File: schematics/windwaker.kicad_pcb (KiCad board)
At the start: 2 copper layers, 2 parts, among them U1 WEMOS_C3_mini, U2 This should be a tft later

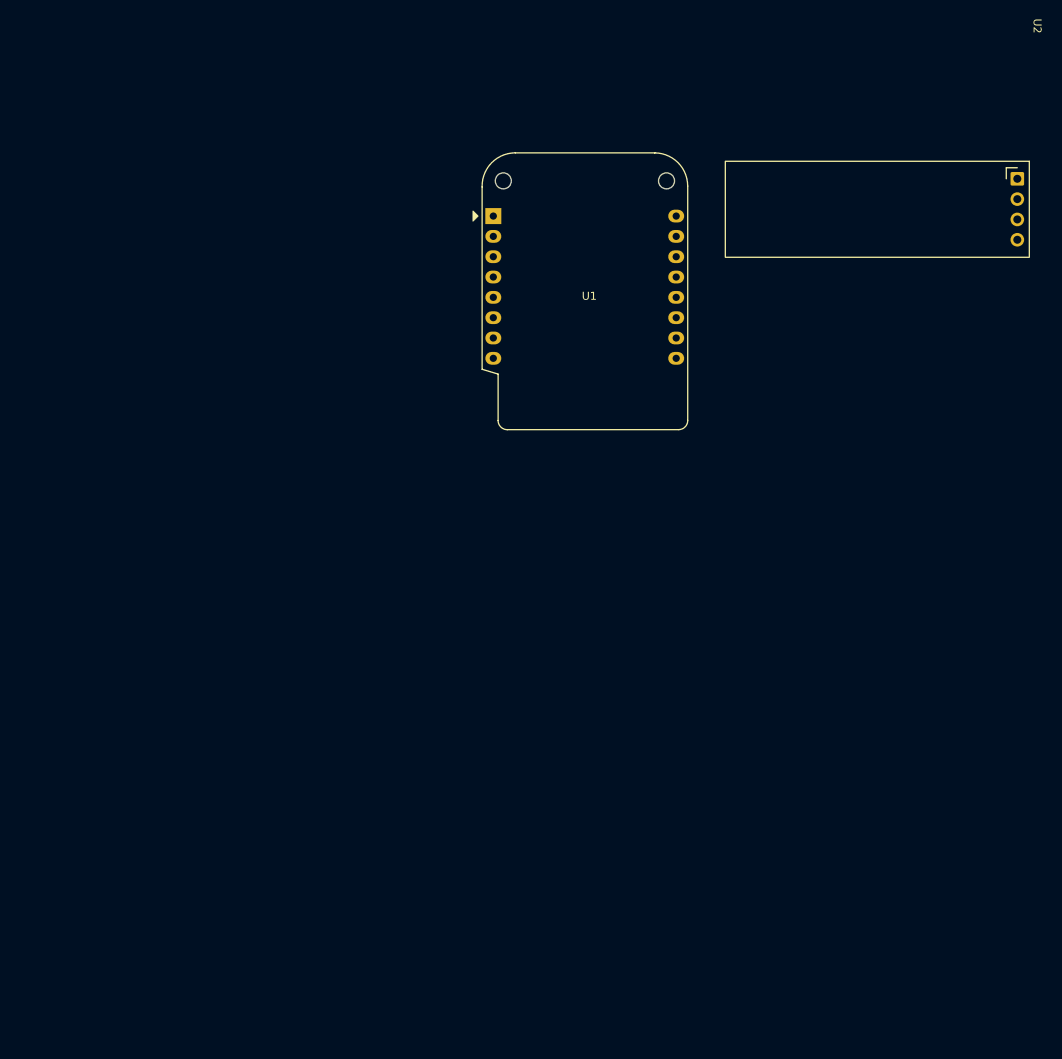
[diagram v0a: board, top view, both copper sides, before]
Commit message: wow, a rough sketch, and a real footprint!
rough sketch by me and footprint for the thing. basic routing can happen now
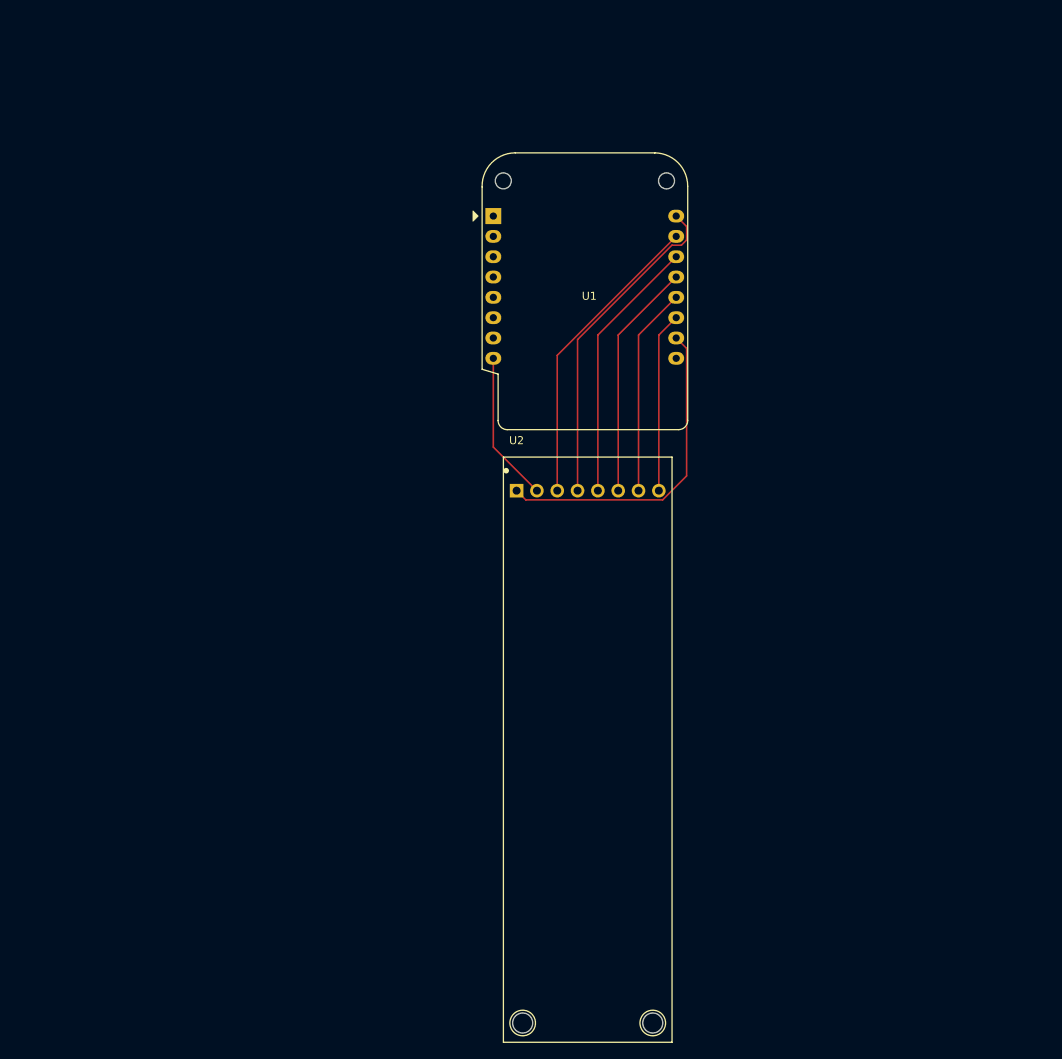
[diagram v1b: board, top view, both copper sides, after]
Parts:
- U2: value This should be a tft later -> TFT Display; footprint Display:ER_OLEDM0.91_1x-I2C -> my_custom_library:TFT-Display_ST7789_2.25in_76x284_8P
- moved U2 73.7 mm to (140.4, 114.7), turned to 0 degrees
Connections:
- U1 pad 10: Net-(BZ1--) -> GND
- U1 pad 11: unconnected-(U1-D6-Pad11) -> Net-(U1-D6)
- U1 pad 12: unconnected-(U1-D7-Pad12) -> Net-(U1-D7)
- U1 pad 13: unconnected-(U1-D8-Pad13) -> Net-(U1-D8)
- U1 pad 14: unconnected-(U1-D10-Pad14) -> Net-(U1-D10)
- U1 pad 8: Net-(BZ1-+) -> +3V3
- U2 pad 1: +3V3 -> GND
- U2 pad 2: GND -> +3V3
- U2 pad 3: Net-(U1-TX) -> Net-(U1-RX)
- U2 pad 4: Net-(U1-RX) -> Net-(U1-TX)
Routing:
- net Net-(U1-TX): track 0.00 -> 41.2 mm
- net GND: track 0.00 -> 40.7 mm
- net Net-(U1-RX): track 0.00 -> 37.9 mm
- net Net-(U1-D10): track 0.00 -> 33.3 mm
- net Net-(U1-D8): track 0.00 -> 29.7 mm
- net Net-(U1-D7): track 0.00 -> 26.1 mm
- net Net-(U1-D6): track 0.00 -> 22.5 mm
- net +3V3: track 0.00 -> 18.8 mm

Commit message: adding some 3d models and routing the pcb
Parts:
- added BZ1: Buzzer, my_custom_library:Buzzer_12x9.5RM7.6, F.Cu at (87.3, 153.2)
- added SW1: SW_Push, Button_Switch_Keyboard:SW_Cherry_MX_1.00u_PCB, F.Cu at (90.0, 130.3)
- added SW2: SW_Push, Button_Switch_Keyboard:SW_Cherry_MX_1.00u_PCB, F.Cu at (90.0, 111.3)
- added SW3: SW_Push, Button_Switch_Keyboard:SW_Cherry_MX_1.00u_PCB, F.Cu at (90.0, 92.2)
- added SW4: SW_Push, Button_Switch_Keyboard:SW_Cherry_MX_1.00u_PCB, F.Cu at (90.0, 73.3)
- U1: moved to B.Cu
- moved U1 40.9 mm to (99.4, 95.2)
- moved U2 37.3 mm to (119.7, 145.8), turned to 180 degrees
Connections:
- U1 pad 3: unconnected-(U1-D2-Pad3) -> Net-(U1-D2)
- U1 pad 4: unconnected-(U1-D1-Pad4) -> Net-(U1-D1)
- U1 pad 5: unconnected-(U1-D0-Pad5) -> Net-(U1-D0)
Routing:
- net GND: track 40.7 -> 161.7 mm
- net +3V3: track 18.8 -> 127.1 mm
- net Net-(U1-D6): track 22.5 -> 71.7 mm
- net Net-(U1-D7): track 26.1 -> 68.1 mm
- net Net-(U1-D3): track 0.00 -> 41.5 mm
- net Net-(U1-D8): track 29.7 -> 64.5 mm
- net Net-(U1-D10): track 33.3 -> 60.9 mm
- net Net-(U1-D2): track 0.00 -> 25.9 mm
- net Net-(U1-RX): track 37.9 -> 56.3 mm
- net Net-(U1-D0): track 0.00 -> 15.7 mm
- net Net-(U1-TX): track 41.2 -> 54.8 mm
- net Net-(U1-D1): track 0.00 -> 11.3 mm
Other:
- board outline added: 46.4 x 93.6 mm

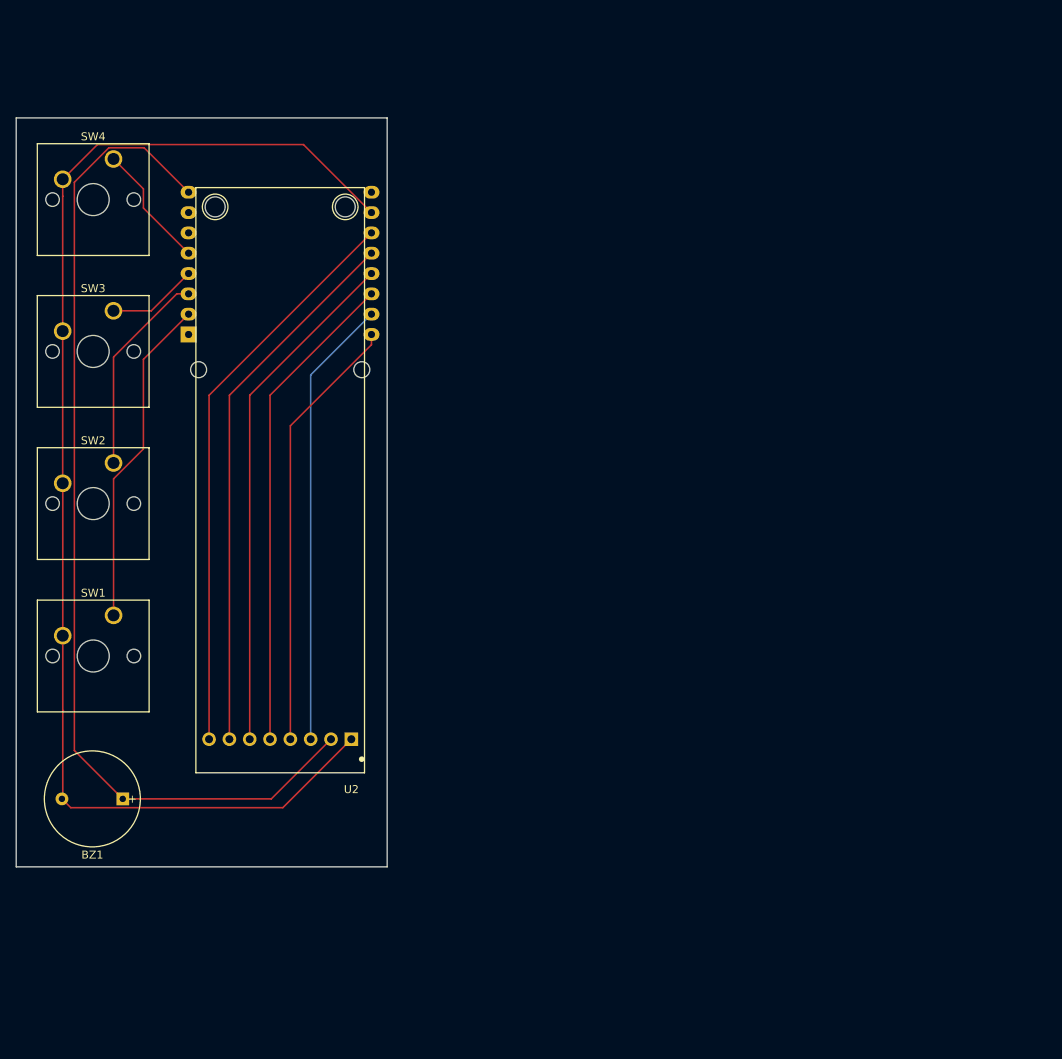
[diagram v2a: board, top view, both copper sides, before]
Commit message: Begin journaling and firmware work
Firmware now has cpp classes for the mx switches,  and a wiring diagram
Also changed up .gitignore to be from the KiCad gitnore from official Github, now containing the .history folder (no more of those yes).
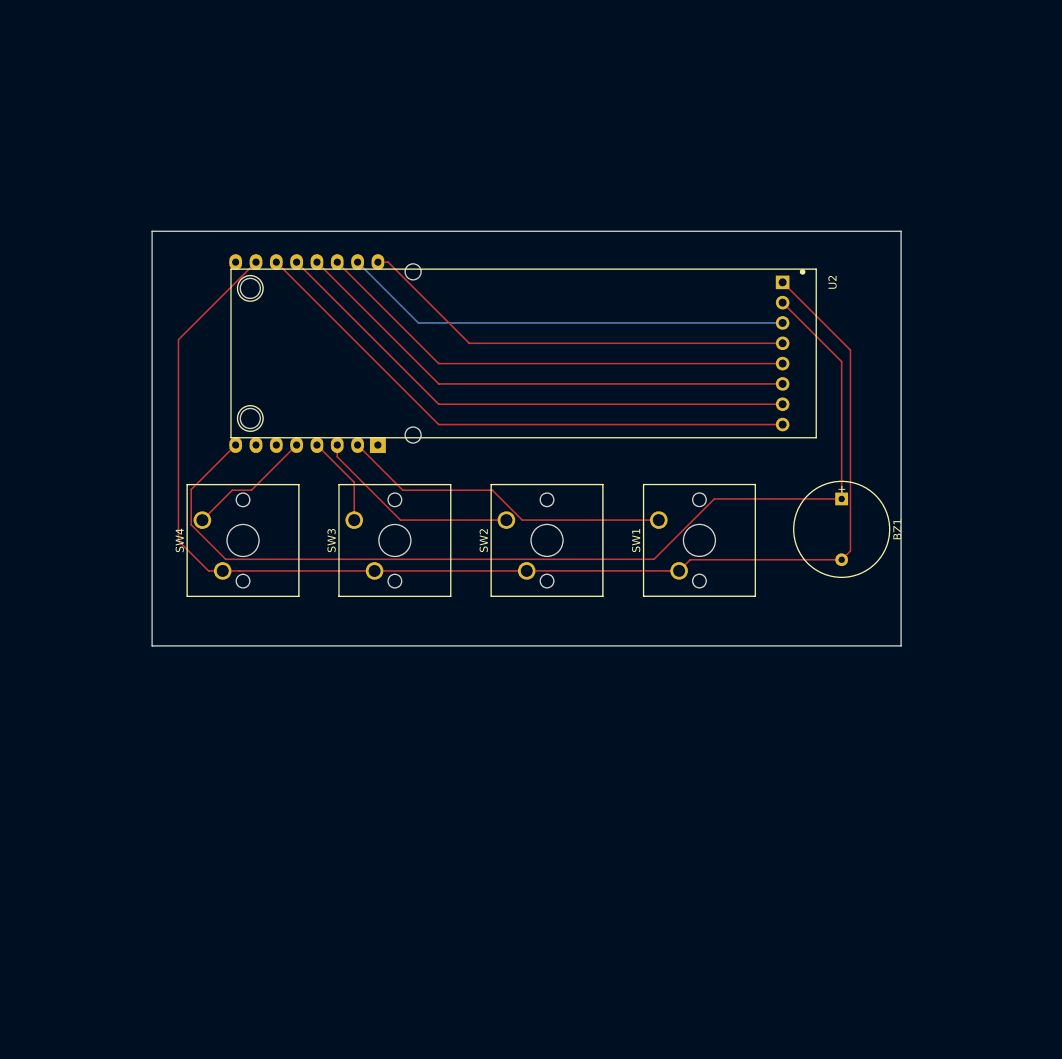
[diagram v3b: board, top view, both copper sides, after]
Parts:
- moved BZ1 99.5 mm to (181.0, 119.6), turned to -90 degrees
- moved U2 78.5 mm to (173.6, 88.7), turned to -90 degrees
- moved SW1 69.2 mm to (158.1, 118.4), turned to 90 degrees
- moved SW2 49.6 mm to (139.1, 118.4), turned to 90 degrees
- moved SW4 46.5 mm to (101.1, 118.4), turned to 90 degrees
- moved SW3 39.9 mm to (120.1, 118.4), turned to 90 degrees
- moved U1 27.4 mm to (123.0, 109.0), turned to 90 degrees
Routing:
- net +3V3: track 127.1 -> 126.1 mm
- net GND: track 161.7 -> 162.5 mm
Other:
- board size 46.4 x 93.6 mm -> 93.6 x 51.8 mm

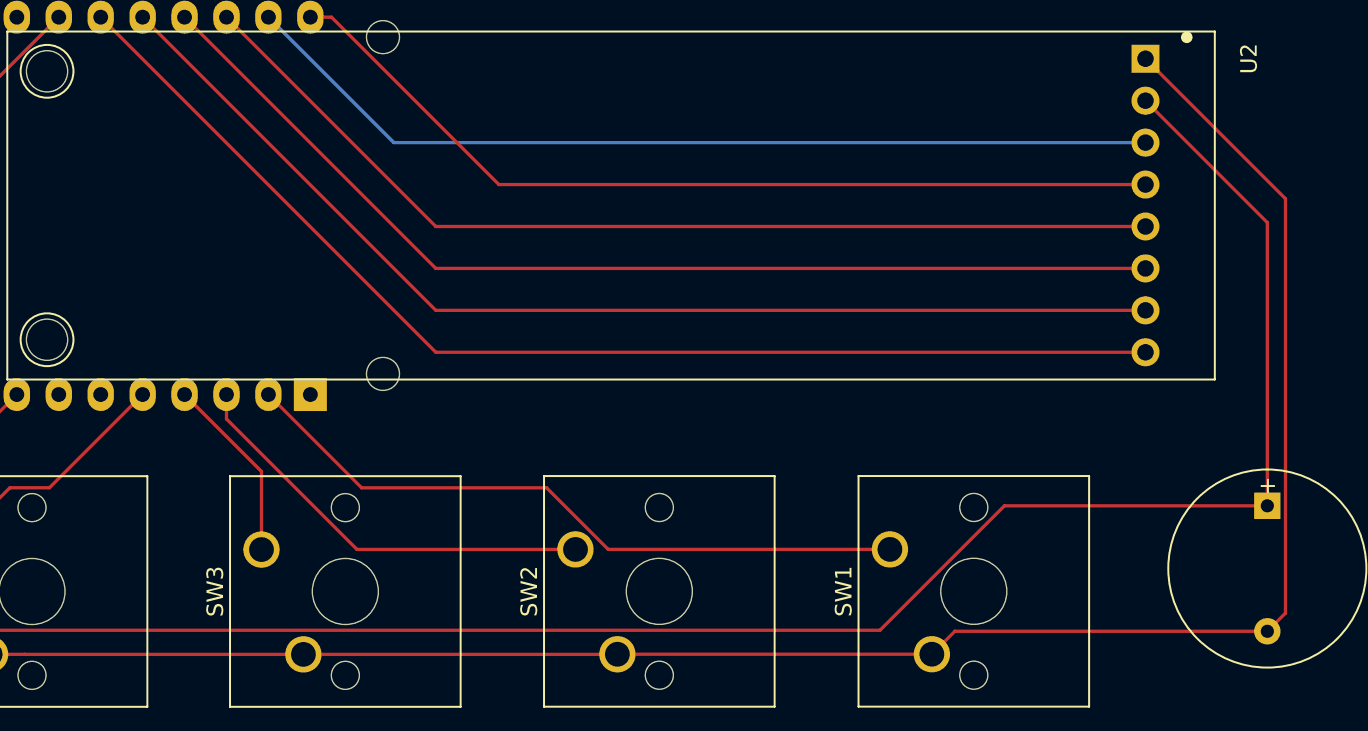
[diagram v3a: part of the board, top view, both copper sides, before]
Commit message: fixed pcb and firmware
buzz should've been with pin
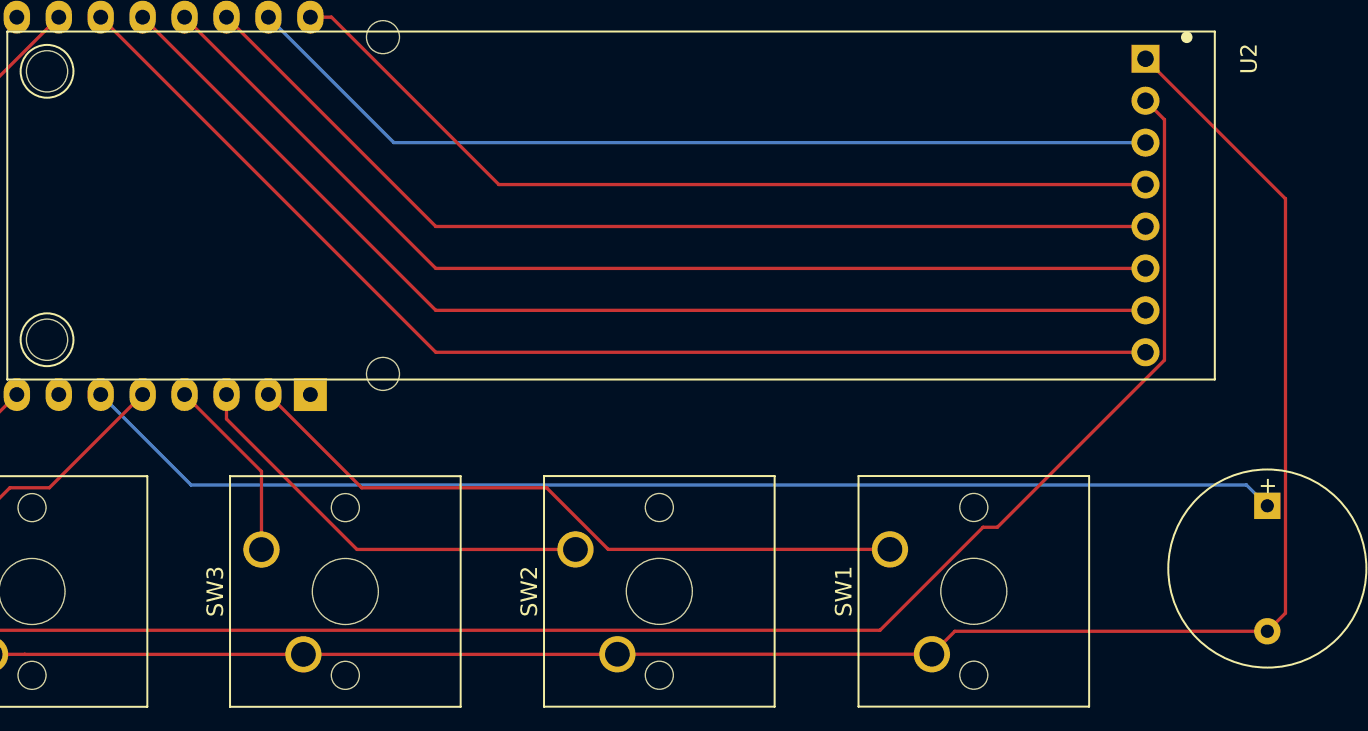
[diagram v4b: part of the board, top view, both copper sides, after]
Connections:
- BZ1 pad 1: +3V3 -> Net-(BZ1-+)
- U1 pad 6: unconnected-(U1-D4-Pad6) -> Net-(BZ1-+)
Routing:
- net Net-(BZ1-+): track 0.00 -> 73.5 mm
- net +3V3: track 126.1 -> 112.1 mm
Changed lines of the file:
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@@
 		(sheetname "/")
 		(sheetfile "windwaker.kicad_sch")
+		(units
+			(unit
+				(name "A")
+				(pins "1" "2")
+			)
+		)
 		(attr through_hole)
 		(duplicate_pad_numbers_are_jumpers no)
@@
 			(layers "*.Cu" "*.Mask")
 			(remove_unused_layers no)
-			(net "+3V3")
+			(net "Net-(BZ1-+)")
 			(pinfunction "+_1")
 			(pintype "passive")
@@
 		(sheetname "/")
 		(sheetfile "windwaker.kicad_sch")
+		(units
+			(unit
+				(name "A")
+				(pins "1" "2")
+			)
+		)
 		(attr through_hole)
 		(duplicate_pad_numbers_are_jumpers no)
@@
 		(sheetname "/")
 		(sheetfile "windwaker.kicad_sch")
+		(units
+			(unit
+				(name "A")
+				(pins "1" "2")
+			)
+		)
 		(attr through_hole)
 		(duplicate_pad_numbers_are_jumpers no)
@@
 		(sheetname "/")
 		(sheetfile "windwaker.kicad_sch")
+		(units
+			(unit
+				(name "A")
+				(pins "1" "2")
+			)
+		)
 		(attr through_hole)
 		(duplicate_pad_numbers_are_jumpers no)
@@
 			(layers "*.Cu" "*.Mask")
 			(remove_unused_layers no)
-			(net "unconnected-(U1-D4-Pad6)")
+			(net "Net-(BZ1-+)")
 			(pinfunction "D4_6")
 			(pintype "bidirectional")
@@
 	)
 	(segment
-		(start 103.994695 123.3)
-		(end 157.531192 123.3)
+		(start 115.804594 114.5)
+		(end 110.324594 109.02)
+		(width 0.2)
+		(layer "B.Cu")
+		(net "Net-(BZ1-+)")
+	)
+	(segment
+		(start 180.994594 115.76)
+		(end 179.734594 114.5)
+		(width 0.2)
+		(layer "B.Cu")
+		(net "Net-(BZ1-+)")
+	)
+	(segment
+		(start 179.734594 114.5)
+		(end 115.804594 114.5)
+		(width 0.2)
+		(layer "B.Cu")
+		(net "Net-(BZ1-+)")
+	)
+	(segment
+		(start 174.764594 92.37)
+		(end 174.764594 106.936346)
 		(width 0.2)
 		(layer "F.Cu")
@@
 	)
 	(segment
-		(start 165.071192 115.76)
-		(end 180.994594 115.76)
+		(start 163.771192 117.06)
+		(end 157.531192 123.3)
 		(width 0.2)
 		(layer "F.Cu")
@@
 	)
 	(segment
-		(start 157.531192 123.3)
-		(end 165.071192 115.76)
+		(start 103.994695 123.3)
+		(end 157.531192 123.3)
 		(width 0.2)
 		(layer "F.Cu")
@@
 	)
 	(segment
-		(start 99.684594 118.989899)
-		(end 103.994695 123.3)
+		(start 173.614594 91.22)
+		(end 174.764594 92.37)
 		(width 0.2)
 		(layer "F.Cu")
@@
 	)
 	(segment
-		(start 180.994594 115.76)
-		(end 180.994594 98.6)
+		(start 99.684594 118.989899)
+		(end 103.994695 123.3)
 		(width 0.2)
 		(layer "F.Cu")
@@
 	)
 	(segment
-		(start 180.994594 98.6)
-		(end 173.614594 91.22)
+		(start 174.764594 106.936346)
+		(end 164.64094 117.06)
 		(width 0.2)
 		(layer "F.Cu")
@@
 		(width 0.2)
 		(layer "F.Cu")
+		(net "+3V3")
+	)
+	(segment
+		(start 164.64094 117.06)
+		(end 163.771192 117.06)
+		(width 0.2)
+		(layer "F.Cu")
